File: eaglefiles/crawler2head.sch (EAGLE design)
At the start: 25 parts, among them U1 PCA9685

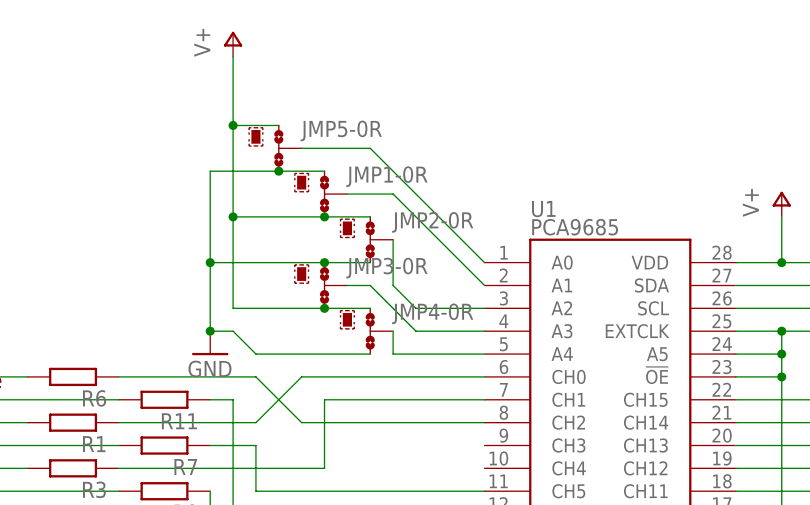
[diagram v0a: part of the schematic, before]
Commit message: fixed wrong chematic for head
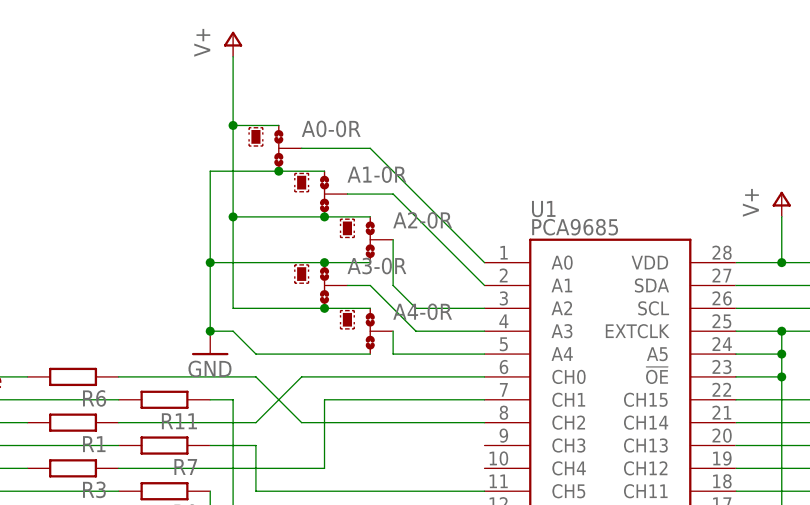
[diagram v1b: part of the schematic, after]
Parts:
- A0: value 0R-JUMPB -> A0
- renumbered JMP1 to A1, JMP2 to A2, JMP3 to A3, JMP4 to A4, JMP5 to A0
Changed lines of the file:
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@@
 <part name="GND1" library="supply1" library_urn="urn:adsk.eagle:library:371" deviceset="GND" device=""/>
 <part name="P+1" library="supply1" library_urn="urn:adsk.eagle:library:371" deviceset="V+" device=""/>
-<part name="JMP1" library="jump-0r-smd" library_urn="urn:adsk.eagle:library:251" deviceset="0R-JUMP" device="B" package3d_urn="urn:adsk.eagle:package:15387/1" value="0R-JUMPB"/>
-<part name="JMP2" library="jump-0r-smd" library_urn="urn:adsk.eagle:library:251" deviceset="0R-JUMP" device="B" package3d_urn="urn:adsk.eagle:package:15387/1" value="0R-JUMPB"/>
-<part name="JMP3" library="jump-0r-smd" library_urn="urn:adsk.eagle:library:251" deviceset="0R-JUMP" device="B" package3d_urn="urn:adsk.eagle:package:15387/1" value="0R-JUMPB"/>
-<part name="JMP4" library="jump-0r-smd" library_urn="urn:adsk.eagle:library:251" deviceset="0R-JUMP" device="B" package3d_urn="urn:adsk.eagle:package:15387/1" value="0R-JUMPB"/>
-<part name="JMP5" library="jump-0r-smd" library_urn="urn:adsk.eagle:library:251" deviceset="0R-JUMP" device="B" package3d_urn="urn:adsk.eagle:package:15387/1" value="0R-JUMPB"/>
+<part name="A1" library="jump-0r-smd" library_urn="urn:adsk.eagle:library:251" deviceset="0R-JUMP" device="B" package3d_urn="urn:adsk.eagle:package:15387/1" value=""/>
+<part name="A2" library="jump-0r-smd" library_urn="urn:adsk.eagle:library:251" deviceset="0R-JUMP" device="B" package3d_urn="urn:adsk.eagle:package:15387/1" value=""/>
+<part name="A3" library="jump-0r-smd" library_urn="urn:adsk.eagle:library:251" deviceset="0R-JUMP" device="B" package3d_urn="urn:adsk.eagle:package:15387/1" value=""/>
+<part name="A4" library="jump-0r-smd" library_urn="urn:adsk.eagle:library:251" deviceset="0R-JUMP" device="B" package3d_urn="urn:adsk.eagle:package:15387/1" value=""/>
+<part name="A0" library="jump-0r-smd" library_urn="urn:adsk.eagle:library:251" deviceset="0R-JUMP" device="B" package3d_urn="urn:adsk.eagle:package:15387/1" value="A0"/>
 </parts>
 <sheets>
@@
 <instance part="GND1" gate="1" x="309.88" y="134.62"/>
 <instance part="P+1" gate="1" x="312.42" y="170.18"/>
-<instance part="JMP1" gate="-0R" x="322.58" y="152.4"/>
-<instance part="JMP1" gate="G$2" x="320.04" y="154.94"/>
-<instance part="JMP2" gate="-0R" x="327.66" y="147.32"/>
-<instance part="JMP2" gate="G$2" x="325.12" y="149.86"/>
-<instance part="JMP3" gate="-0R" x="322.58" y="142.24"/>
-<instance part="JMP3" gate="G$2" x="320.04" y="144.78"/>
-<instance part="JMP4" gate="-0R" x="327.66" y="137.16"/>
-<instance part="JMP4" gate="G$2" x="325.12" y="139.7"/>
-<instance part="JMP5" gate="-0R" x="317.5" y="157.48"/>
-<instance part="JMP5" gate="G$2" x="314.96" y="160.02"/>
+<instance part="A1" gate="-0R" x="322.58" y="152.4"/>
+<instance part="A1" gate="G$2" x="320.04" y="154.94"/>
+<instance part="A2" gate="-0R" x="327.66" y="147.32"/>
+<instance part="A2" gate="G$2" x="325.12" y="149.86"/>
+<instance part="A3" gate="-0R" x="322.58" y="142.24"/>
+<instance part="A3" gate="G$2" x="320.04" y="144.78"/>
+<instance part="A4" gate="-0R" x="327.66" y="137.16"/>
+<instance part="A4" gate="G$2" x="325.12" y="139.7"/>
+<instance part="A0" gate="-0R" x="317.5" y="157.48"/>
+<instance part="A0" gate="G$2" x="314.96" y="160.02"/>
 </instances>
 <busses>
@@
 </segment>
 <segment>
-<pinref part="JMP1" gate="-0R" pin="1"/>
-<pinref part="JMP5" gate="-0R" pin="3"/>
+<pinref part="A1" gate="-0R" pin="1"/>
+<pinref part="A0" gate="-0R" pin="3"/>
 <wire x1="322.58" y1="154.94" x2="317.5" y2="154.94" width="0.1524" layer="91"/>
 <pinref part="GND1" gate="1" pin="GND"/>
@@
 <wire x1="309.88" y1="154.94" x2="309.88" y2="144.78" width="0.1524" layer="91"/>
 <junction x="317.5" y="154.94"/>
-<pinref part="JMP2" gate="-0R" pin="3"/>
-<pinref part="JMP3" gate="-0R" pin="1"/>
+<pinref part="A2" gate="-0R" pin="3"/>
+<pinref part="A3" gate="-0R" pin="1"/>
 <wire x1="309.88" y1="144.78" x2="309.88" y2="137.16" width="0.1524" layer="91"/>
 <wire x1="327.66" y1="144.78" x2="322.58" y2="144.78" width="0.1524" layer="91"/>
@@
 <junction x="322.58" y="144.78"/>
 <junction x="309.88" y="144.78"/>
-<pinref part="JMP4" gate="-0R" pin="3"/>
+<pinref part="A4" gate="-0R" pin="3"/>
 <wire x1="327.66" y1="134.62" x2="314.96" y2="134.62" width="0.1524" layer="91"/>
 <wire x1="314.96" y1="134.62" x2="312.42" y2="137.16" width="0.1524" layer="91"/>
@@
 </segment>
 <segment>
-<pinref part="JMP5" gate="-0R" pin="1"/>
+<pinref part="A0" gate="-0R" pin="1"/>
 <pinref part="P+1" gate="1" pin="V+"/>
 <wire x1="317.5" y1="160.02" x2="312.42" y2="160.02" width="0.1524" layer="91"/>
 <wire x1="312.42" y1="160.02" x2="312.42" y2="167.64" width="0.1524" layer="91"/>
-<pinref part="JMP2" gate="-0R" pin="1"/>
-<pinref part="JMP1" gate="-0R" pin="3"/>
+<pinref part="A2" gate="-0R" pin="1"/>
+<pinref part="A1" gate="-0R" pin="3"/>
 <wire x1="327.66" y1="149.86" x2="322.58" y2="149.86" width="0.1524" layer="91"/>
 <wire x1="322.58" y1="149.86" x2="312.42" y2="149.86" width="0.1524" layer="91"/>
@@
 <junction x="322.58" y="149.86"/>
 <junction x="312.42" y="160.02"/>
-<pinref part="JMP4" gate="-0R" pin="1"/>
-<pinref part="JMP3" gate="-0R" pin="3"/>
+<pinref part="A4" gate="-0R" pin="1"/>
+<pinref part="A3" gate="-0R" pin="3"/>
 <wire x1="327.66" y1="139.7" x2="322.58" y2="139.7" width="0.1524" layer="91"/>
 <wire x1="322.58" y1="139.7" x2="312.42" y2="139.7" width="0.1524" layer="91"/>
@@
 <segment>
 <pinref part="U1" gate="G$1" pin="A4"/>
-<pinref part="JMP4" gate="-0R" pin="2"/>
+<pinref part="A4" gate="-0R" pin="2"/>
 <wire x1="340.36" y1="134.62" x2="330.2" y2="134.62" width="0.1524" layer="91"/>
 <wire x1="330.2" y1="134.62" x2="330.2" y2="137.16" width="0.1524" layer="91"/>
@@
 <wire x1="340.36" y1="137.16" x2="332.74" y2="137.16" width="0.1524" layer="91"/>
 <wire x1="332.74" y1="137.16" x2="327.66" y2="142.24" width="0.1524" layer="91"/>
-<pinref part="JMP3" gate="-0R" pin="2"/>
+<pinref part="A3" gate="-0R" pin="2"/>
 <wire x1="327.66" y1="142.24" x2="325.12" y2="142.24" width="0.1524" layer="91"/>
 </segment>
@@
 <pinref part="U1" gate="G$1" pin="A2"/>
 <wire x1="340.36" y1="139.7" x2="332.74" y2="139.7" width="0.1524" layer="91"/>
-<pinref part="JMP2" gate="-0R" pin="2"/>
+<pinref part="A2" gate="-0R" pin="2"/>
 <wire x1="332.74" y1="139.7" x2="330.2" y2="142.24" width="0.1524" layer="91"/>
 <wire x1="330.2" y1="142.24" x2="330.2" y2="147.32" width="0.1524" layer="91"/>
@@
 <segment>
 <pinref part="U1" gate="G$1" pin="A1"/>
-<pinref part="JMP1" gate="-0R" pin="2"/>
+<pinref part="A1" gate="-0R" pin="2"/>
 <wire x1="340.36" y1="142.24" x2="330.2" y2="152.4" width="0.1524" layer="91"/>
 <wire x1="330.2" y1="152.4" x2="325.12" y2="152.4" width="0.1524" layer="91"/>
@@
 <segment>
 <pinref part="U1" gate="G$1" pin="A0"/>
-<pinref part="JMP5" gate="-0R" pin="2"/>
+<pinref part="A0" gate="-0R" pin="2"/>
 <wire x1="340.36" y1="144.78" x2="327.66" y2="157.48" width="0.1524" layer="91"/>
 <wire x1="327.66" y1="157.48" x2="320.04" y2="157.48" width="0.1524" layer="91"/>
